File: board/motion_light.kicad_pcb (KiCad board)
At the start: 2 copper layers, 35 x 64 mm, 22 parts, among them CON1 AVR-ISP-6, J1 MOTION, J2 Conn_01x05, Q1 BSS83P, SW1 SW_Push, SW2 SW_Push, U1 ATTINY84A-SSU, U2 APA102, U3 APA102, U4 PIR_MODULE

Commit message: Moar schematic changes
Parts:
- added J3: USB_OTG, Connectors_USB:USB_Micro-B_Molex-105017-0001, F.Cu at (131.5, 122.2)
- moved R3 11.7 mm to (125.5, 83.3)
- moved Q1 9.20 mm to (136.7, 85.0)
- moved REF*** 4.00 mm to (131.5, 103.0)
- moved D1 2.40 mm to (116.8, 92.0), turned to 180 degrees
- moved R4 1.90 mm to (128.2, 83.3), turned to 270 degrees
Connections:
- J1 pad 2: VCC -> /ACC_PWR
- U4 pad 1: VCC -> /ACC_PWR
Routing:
- net /ACC_PWR: track 48.0 -> 71.1 mm, vias 2 -> 3
- net /STATUS_LED: track 31.2 -> 41.7 mm
- net GND: track 20.0 -> 28.7 mm, vias 6 -> 5
- net Net-(D1-Pad1): track 4.10 -> 11.0 mm, vias 0 -> 2
- net /~ACC_PWR_EN: track 17.9 -> 14.0 mm, vias 2 -> 0
- net VCC: track 6.78 -> 10.3 mm, vias 1 -> 0
- net /MOTION: track 50.0 -> 47.3 mm
- net /BUTTON2: track 36.9 -> 38.1 mm
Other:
- outline, holes or cut-outs redrawn
- board text added: "(Power only)"

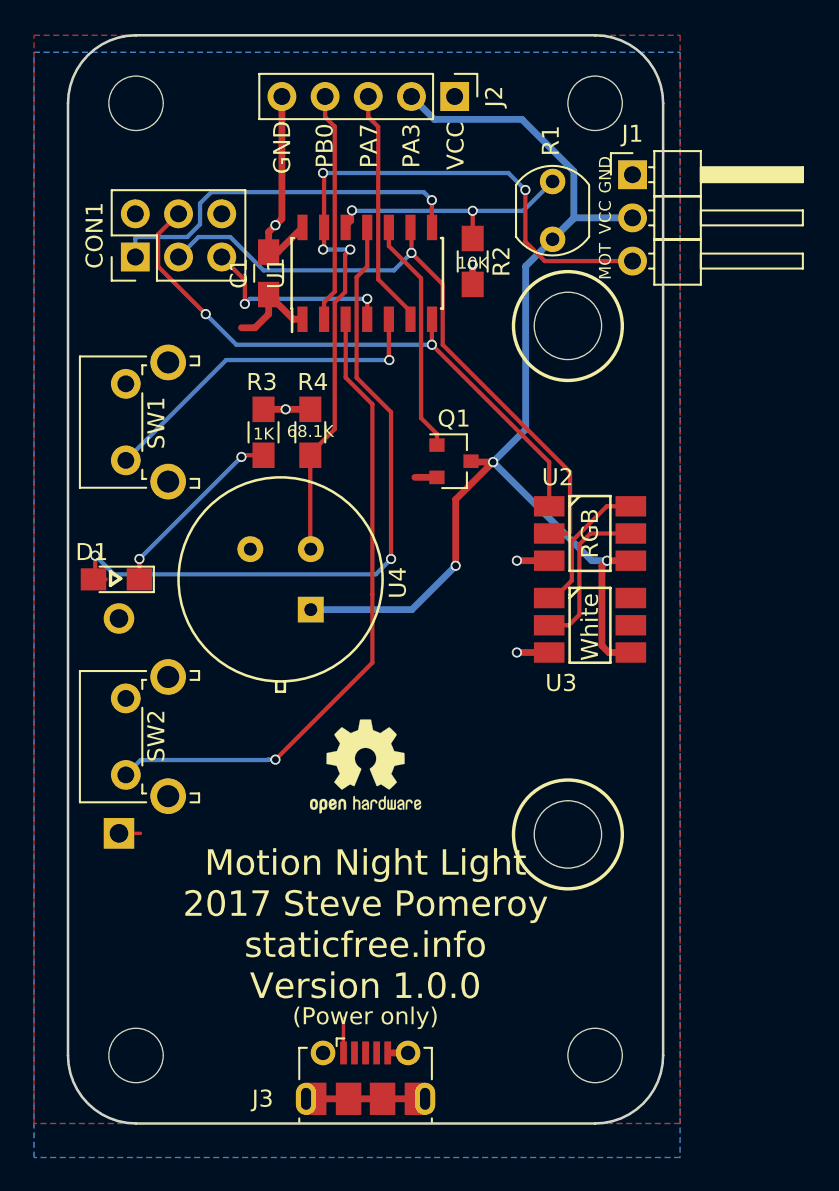
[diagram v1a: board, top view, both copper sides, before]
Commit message: Switch to KiCAD 5; add USB plugs
* Update footprints and library symbols to KiCAD 5
* Add optional USB plugs to power directly
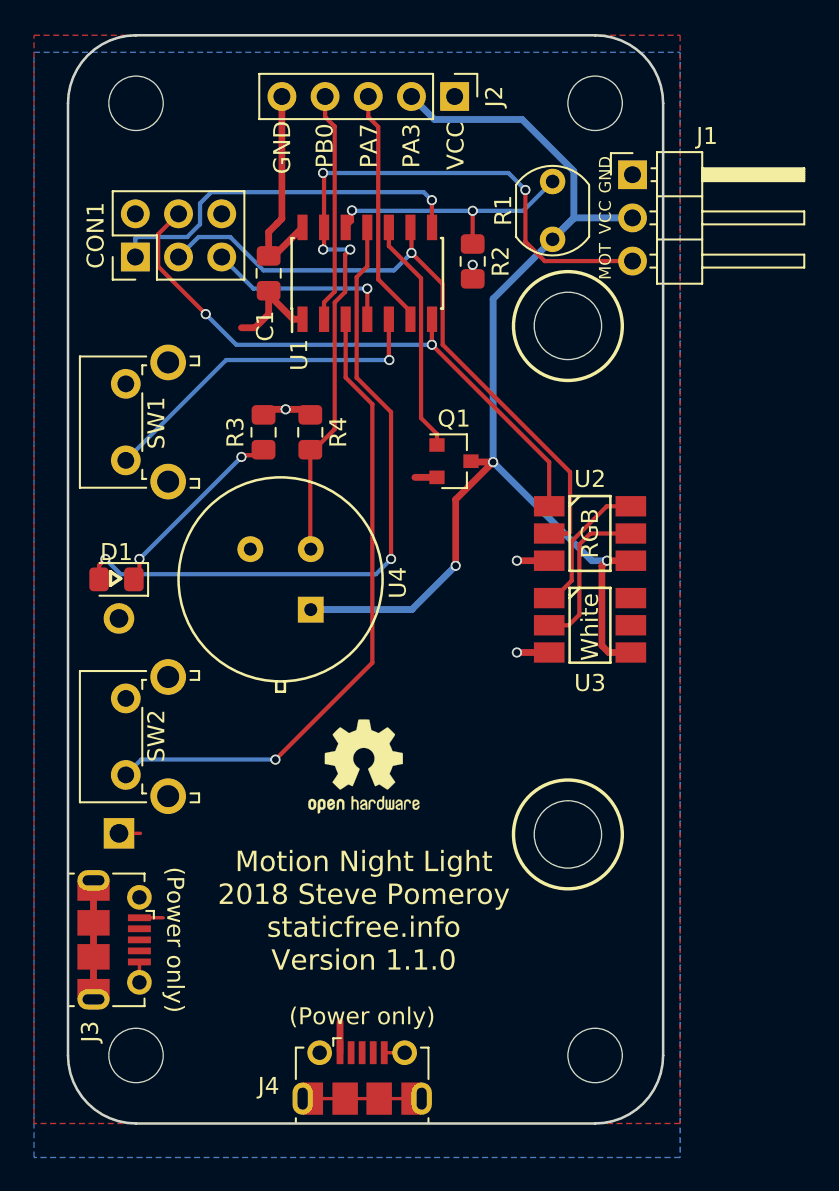
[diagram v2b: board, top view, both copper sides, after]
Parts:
- added J4: USB_MICRO, Connector_USB:USB_Micro-B_Molex-105017-0001, F.Cu at (131.3, 121.3)
- C1: footprint Capacitors_SMD:C_0805_HandSoldering -> Capacitor_SMD:C_0805_2012Metric_Pad1.15x1.40mm_HandSolder
- CON1: footprint Pin_Headers:Pin_Header_Straight_2x03_Pitch2.54mm -> Connector_PinHeader_2.54mm:PinHeader_2x03_P2.54mm_Vertical
- D1: footprint LEDs:LED_0805_HandSoldering -> LED_SMD:LED_0805_2012Metric_Pad1.15x1.40mm_HandSolder
- J1: footprint Pin_Headers:Pin_Header_Angled_1x03_Pitch2.54mm -> Connector_PinHeader_2.54mm:PinHeader_1x03_P2.54mm_Horizontal
- J2: footprint Pin_Headers:Pin_Header_Straight_1x05_Pitch2.54mm -> Connector_PinHeader_2.54mm:PinHeader_1x05_P2.54mm_Vertical
- J3: value USB_OTG -> USB_MICRO; footprint Connectors_USB:USB_Micro-B_Molex-105017-0001 -> Connector_USB:USB_Micro-B_Molex-105017-0001
- Q1: footprint TO_SOT_Packages_SMD:SOT-23 -> Package_TO_SOT_SMD:SOT-23
- R1: footprint Opto-Devices:Resistor_LDR_5.1x4.3_RM3.4 -> OptoDevice:R_LDR_5.1x4.3mm_P3.4mm_Vertical
- R2, R3, R4: footprint Resistors_SMD:R_0805_HandSoldering -> Resistor_SMD:R_0805_2012Metric_Pad1.15x1.40mm_HandSolder
- SW1, SW2: footprint Buttons_Switches_THT:SW_Tactile_SPST_Angled_PTS645Vx83-2LFS -> Button_Switch_THT:SW_Tactile_SPST_Angled_PTS645Vx83-2LFS
- U1: footprint Housings_SOIC:SOIC-14_3.9x8.7mm_Pitch1.27mm -> Package_SO:SOIC-14_3.9x8.7mm_P1.27mm
- moved J3 17.3 mm to (116.7, 113.2), turned to 270 degrees
- moved REF*** 0.10 mm to (131.4, 103.0)
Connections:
- J3 pad 2: (no net) -> Net-(J3-Pad2)
- J3 pad 3: (no net) -> Net-(J3-Pad3)
- J3 pad 4: (no net) -> Net-(J3-Pad4)
- U3 pad 5: (no net) -> Net-(U3-Pad5)
- U3 pad 6: (no net) -> Net-(U3-Pad6)
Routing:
- net GND: track 28.7 -> 35.6 mm, vias 5 -> 4
- net VCC: track 10.3 -> 11.5 mm
- net /AMBIENT: track 16.4 -> 15.4 mm
- net /RESET: track 11.8 -> 11.1 mm, vias 2 -> 1
- net /STATUS_LED: track 41.7 -> 41.1 mm
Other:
- board text added: "Motion Night Light 2018 Steve Pomeroy staticfree.info Version 1.1.0"
- board text removed: "Motion Night Light 2017 Steve Pomeroy staticfree.info Version 1.0.0"
